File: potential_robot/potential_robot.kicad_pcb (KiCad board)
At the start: 2 copper layers, 8 parts, among them U1 LM741, U2 LM741

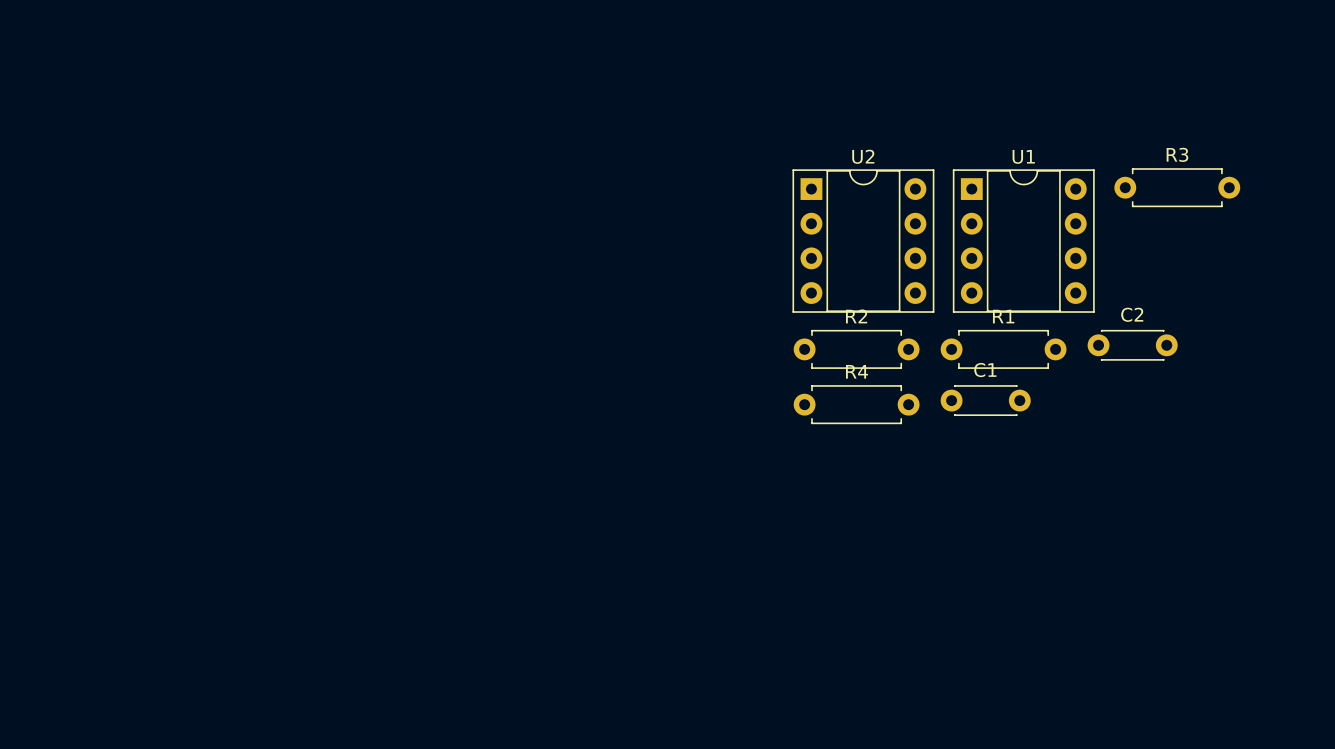
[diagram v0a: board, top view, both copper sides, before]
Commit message: Replaced a resistor with a pot for volume control. Added a power jack, rectifier and smoother TBD.
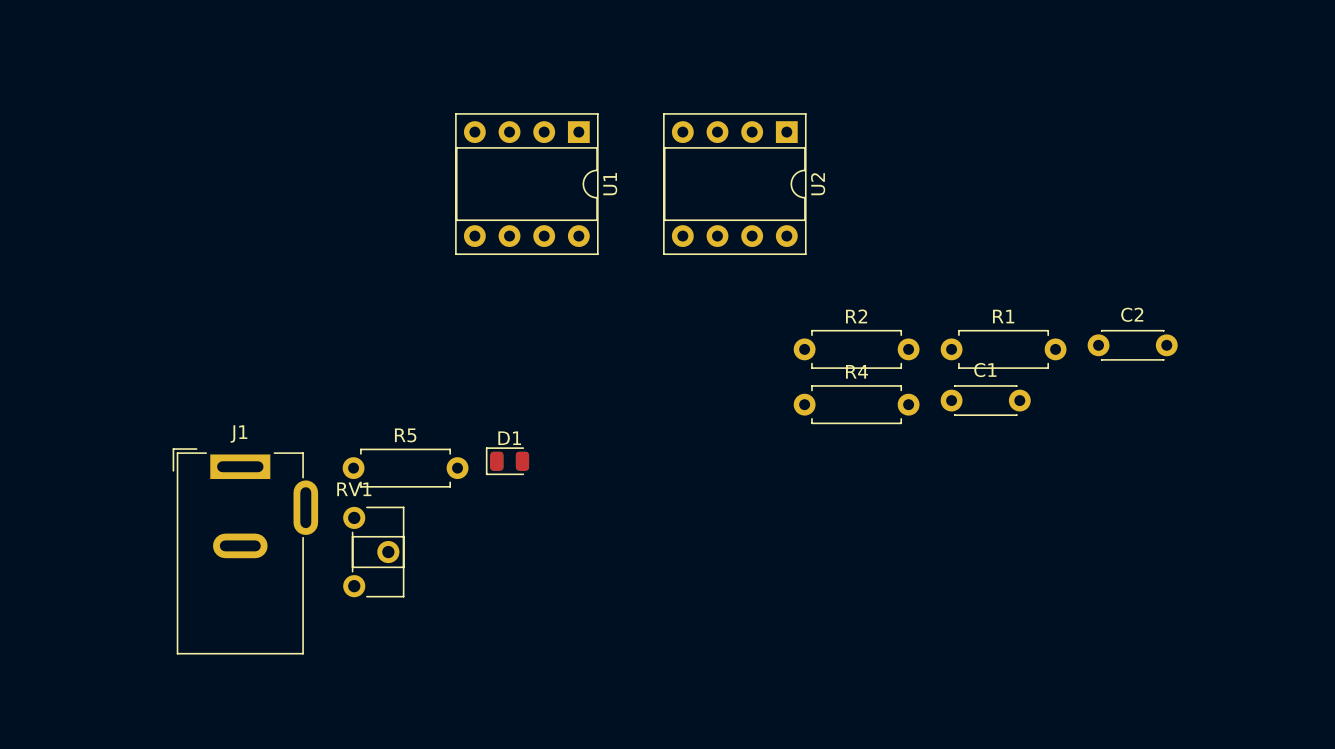
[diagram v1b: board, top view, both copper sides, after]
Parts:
- removed R3: R_US, Resistor_THT:R_Axial_DIN0207_L6.3mm_D2.5mm_P7.62mm_Horizontal
- added D1: LED, LED_SMD:LED_0805_2012Metric, F.Cu at (100.3, 95.2)
- added J1: Barrel_Jack, Connector_BarrelJack:BarrelJack_Wuerth_6941xx301002, F.Cu at (80.6, 95.7)
- added R5: R_US, Resistor_THT:R_Axial_DIN0207_L6.3mm_D2.5mm_P7.62mm_Horizontal, F.Cu at (88.9, 95.8)
- added RV1: 1k, Potentiometer_THT:Potentiometer_ACP_CA6-H2,5_Horizontal, F.Cu at (88.9, 99.4)
- R4: value R_US -> 100
- moved U1 29.1 mm to (105.4, 71.1), turned to -90 degrees
- moved U2 4.55 mm to (120.6, 71.1), turned to -90 degrees

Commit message: added edge cut to pcb
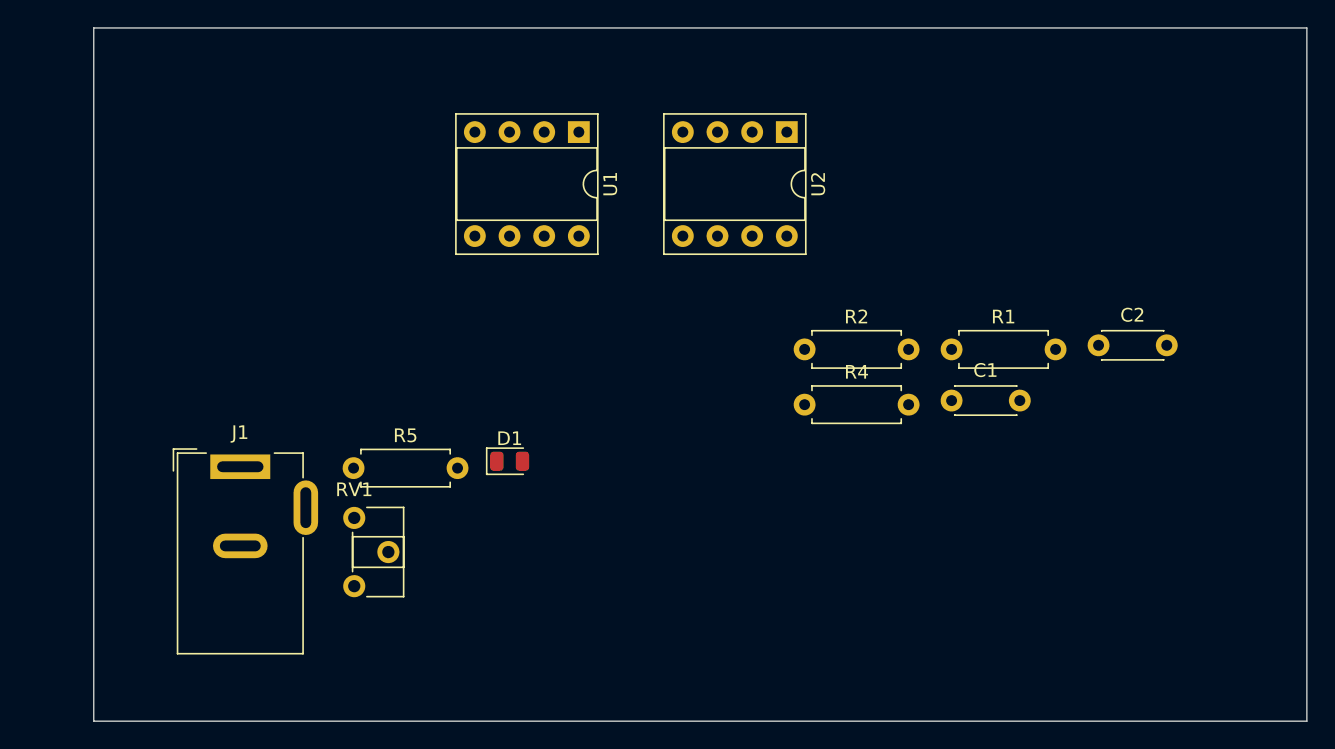
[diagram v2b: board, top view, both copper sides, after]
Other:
- board outline added: 88.9 x 50.8 mm
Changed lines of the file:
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@@
     )
   )
+  (gr_rect (start 69.85 63.5) (end 158.75 114.3) (layer "Edge.Cuts") (width 0.1) (fill none))
 )

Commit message: added a trace
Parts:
- moved J1 26.5 mm to (78.7, 69.2), turned to -90 degrees
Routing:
- net GND: track 0.00 -> 65.6 mm
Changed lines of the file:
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@@
   )
   (footprint "Connector_BarrelJack:BarrelJack_Wuerth_6941xx301002" (layer "F.Cu")
-    (at 80.59 95.655)
+    (at 78.74 69.25 -90)
     (descr "Wuerth electronics barrel jack connector (5.5mm outher diameter, inner diameter 2.05mm or 2.55mm depending on exact order number), See: http://katalog.we-online.de/em/datasheet/6941xx301002.pdf")
     (tags "connector barrel jack")
@@
     (property "Sheetname" "")
     (attr through_hole)
-    (fp_text reference "J1" (at 0 -2.5) (layer "F.SilkS")
-      (effects (font (size 1 1) (thickness 0.15)))
-    )
-    (fp_text value "Barrel_Jack" (at 0 15.5) (layer "F.Fab")
-      (effects (font (size 1 1) (thickness 0.15)))
-    )
-    (fp_text user "${REFERENCE}" (at 0 7.5) (layer "F.Fab")
+    (fp_text reference "J1" (at 0 -2.5 90) (layer "F.SilkS")
+      (effects (font (size 1 1) (thickness 0.15)))
+    )
+    (fp_text value "Barrel_Jack" (at 0 15.5 90) (layer "F.Fab")
+      (effects (font (size 1 1) (thickness 0.15)))
+    )
+    (fp_text user "${REFERENCE}" (at 0 7.5 90) (layer "F.Fab")
       (effects (font (size 1 1) (thickness 0.15)))
     )
@@
     (fp_line (start 4.5 13.6) (end -4.5 13.6) (layer "F.Fab") (width 0.1))
     (fp_line (start 4.5 -0.9) (end -3.5 -0.9) (layer "F.Fab") (width 0.1))
-    (pad "1" thru_hole rect locked (at 0 0) (size 4.4 1.8) (drill oval 3.4 0.8) (layers *.Cu *.Mask)
+    (pad "1" thru_hole rect locked (at 0 0 270) (size 4.4 1.8) (drill oval 3.4 0.8) (layers *.Cu *.Mask)
       (net 17 "AC") (pintype "passive"))
-    (pad "2" thru_hole oval locked (at 0 5.8) (size 4 1.8) (drill oval 3 0.8) (layers *.Cu *.Mask)
+    (pad "2" thru_hole oval locked (at 0 5.8 270) (size 4 1.8) (drill oval 3 0.8) (layers *.Cu *.Mask)
       (net 6 "GND") (pintype "passive"))
-    (pad "3" thru_hole oval locked (at 4.8 3 90) (size 4 1.8) (drill oval 3 0.8) (layers *.Cu *.Mask))
+    (pad "3" thru_hole oval locked (at 4.8 3) (size 4 1.8) (drill oval 3 0.8) (layers *.Cu *.Mask))
     (model "${KICAD6_3DMODEL_DIR}/Connector_BarrelJack.3dshapes/BarrelJack_Wuerth_6941xx301002.wrl"
       (offset (xyz 0 0 0))
@@
   )
   (gr_rect (start 69.85 63.5) (end 158.75 114.3) (layer "Edge.Cuts") (width 0.1) (fill none))
+  (segment (start 72.39 83.82) (end 80.01 91.44) (width 0.25) (layer "F.Cu") (net 6))
+  (segment (start 72.39 74.631732) (end 72.39 83.82) (width 0.25) (layer "F.Cu") (net 6))
+  (segment (start 72.94 69.25) (end 72.94 74.081732) (width 0.25) (layer "F.Cu") (net 6))
+  (segment (start 88.94 104.405) (end 96.255 104.405) (width 0.25) (layer "F.Cu") (net 6))
+  (segment (start 99.3925 93.0425) (end 99.3925 95.25) (width 0.25) (layer "F.Cu") (net 6))
+  (segment (start 99.3925 101.2675) (end 99.3925 95.25) (width 0.25) (layer "F.Cu") (net 6))
+  (segment (start 72.94 74.081732) (end 72.39 74.631732) (width 0.25) (layer "F.Cu") (net 6))
+  (segment (start 96.255 104.405) (end 99.3925 101.2675) (width 0.25) (layer "F.Cu") (net 6))
+  (segment (start 80.01 91.44) (end 97.79 91.44) (width 0.25) (layer "F.Cu") (net 6))
+  (segment (start 97.79 91.44) (end 99.3925 93.0425) (width 0.25) (layer "F.Cu") (net 6))
 )
